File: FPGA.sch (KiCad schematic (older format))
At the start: 8 parts, among them U13 ADS1015, U14 SiT8008B, U8 GW1N-9LQ100

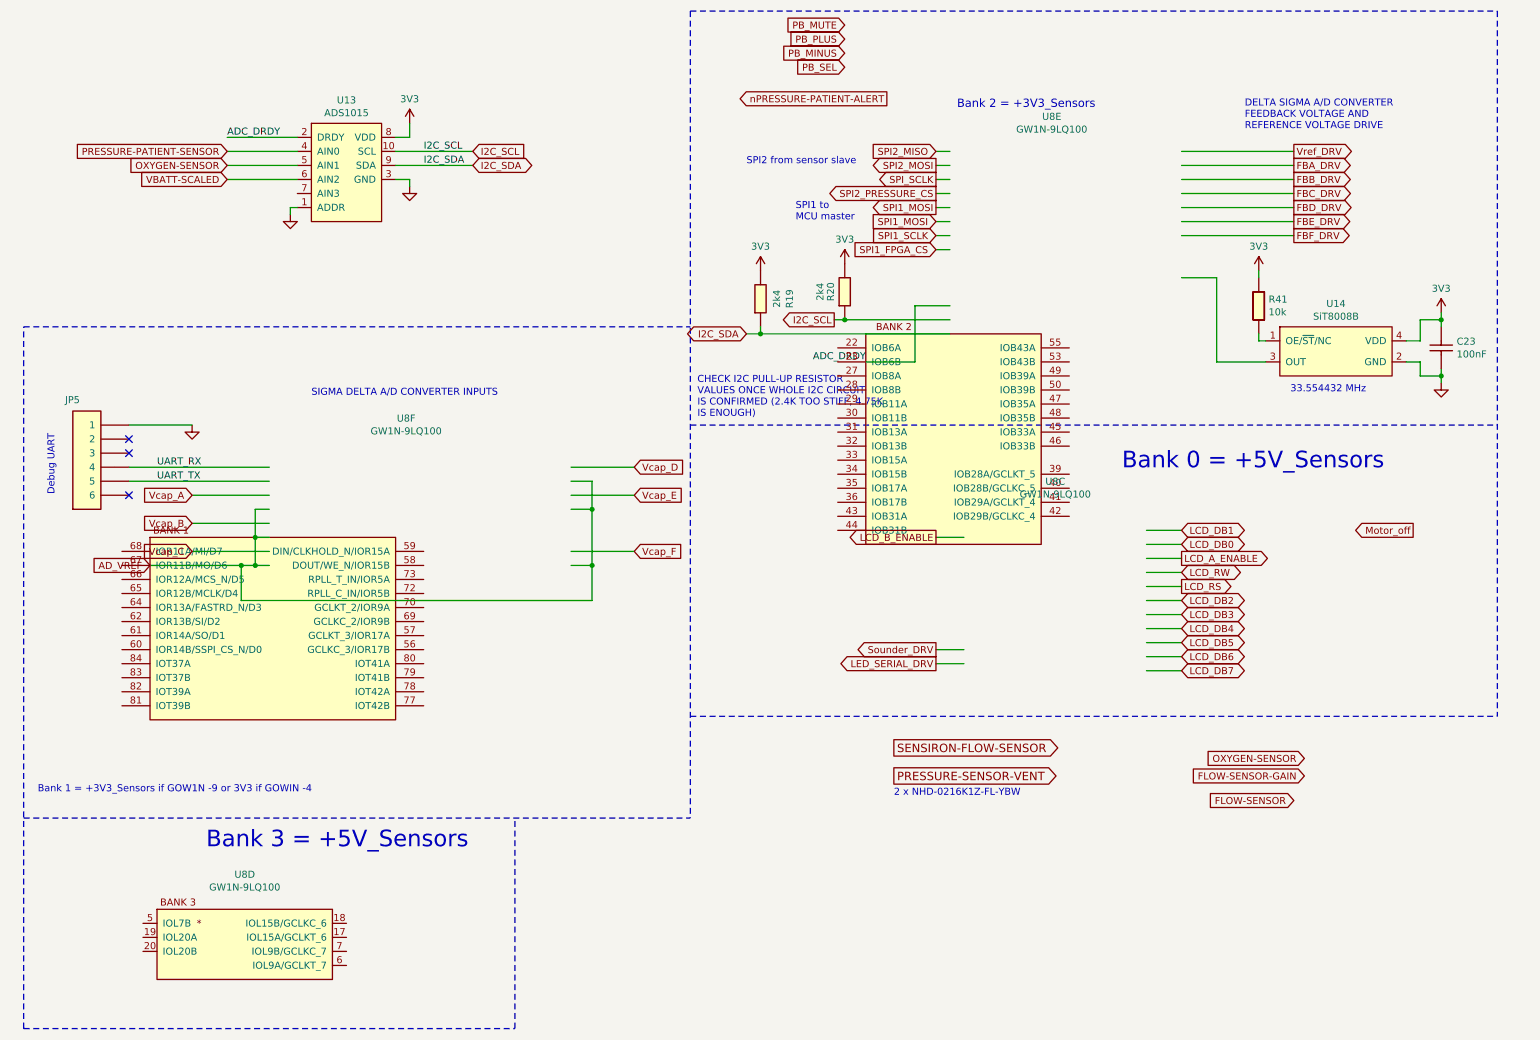
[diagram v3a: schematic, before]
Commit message: Update FPGA symbol, remove FPGA_trial sheet
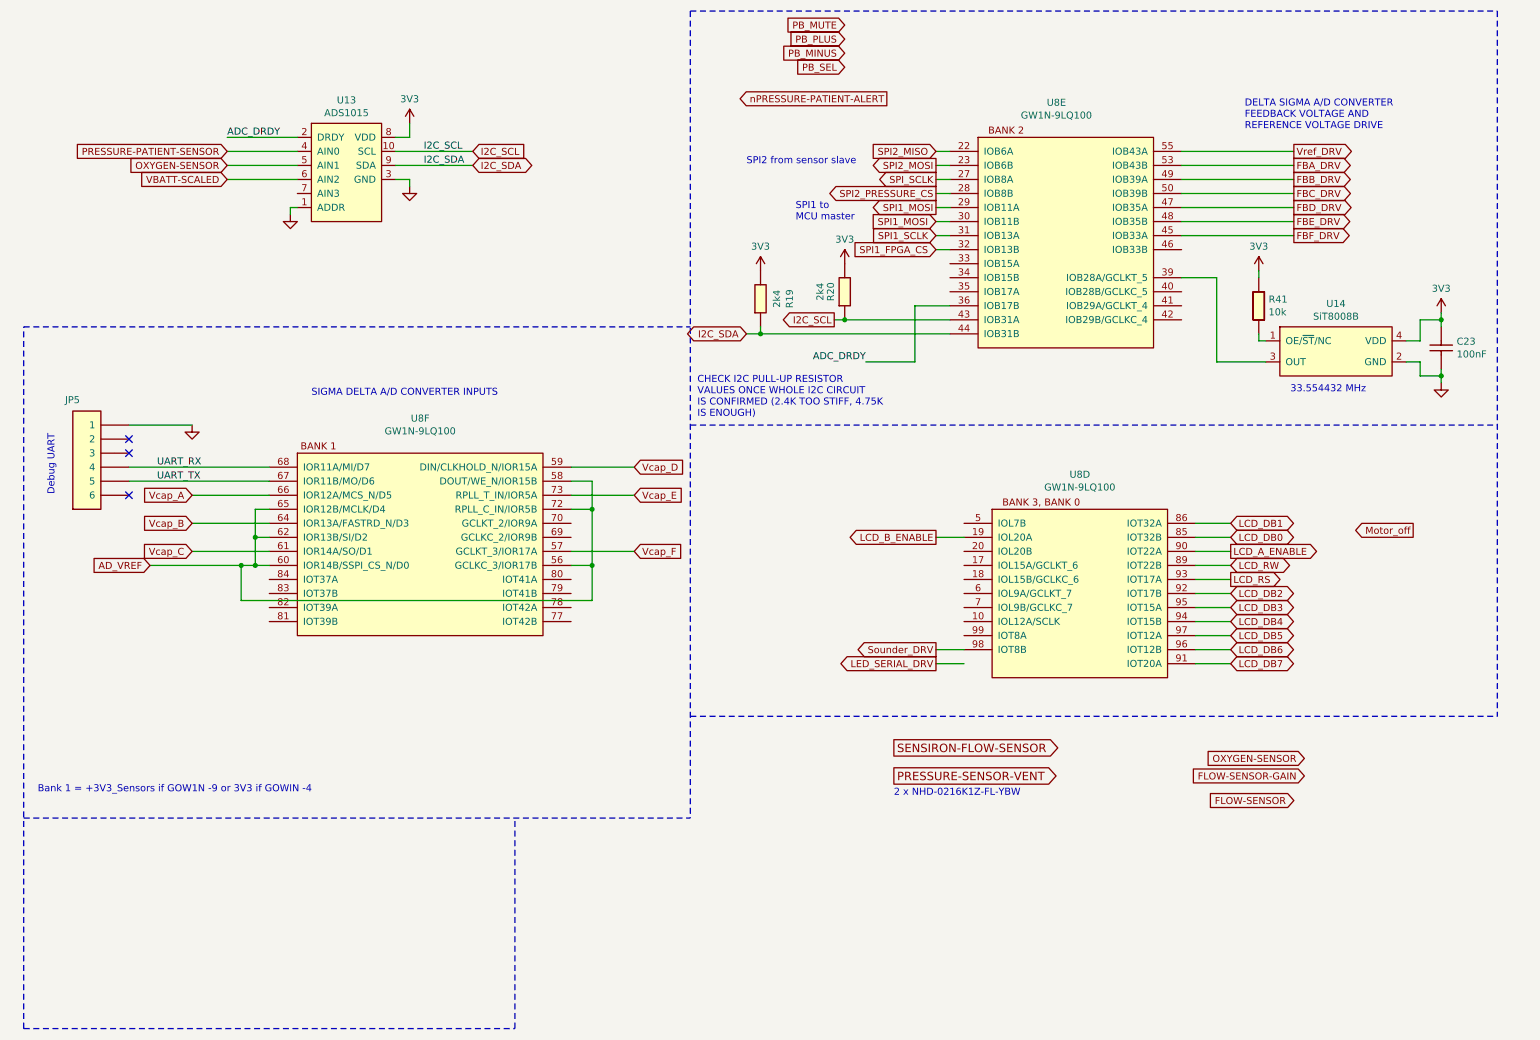
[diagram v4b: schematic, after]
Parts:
- removed unit 4 of U8
- removed unit 3 of U8
- added unit 4 of U8
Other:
- note removed: "Bank 0 = +5V_Sensors"
- note removed: "Bank 2 = +3V3_Sensors\n"
- note removed: "Bank 3 = +5V_Sensors"
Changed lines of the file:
@@
 $Descr A4 11693 8268
 encoding utf-8
-Sheet 6 10
+Sheet 6 9
 Title "OpenVent Control Board"
 Date "2020-10-20"
@@
 PRESSURE-PATIENT-SENSOR
 $Comp
-L OpenVent:GW1N-9LQ100 U8
-U 6 1 5FCFFCE4
-P 2250 4250
-AR Path="/5FCFFCE4" Ref="U8"  Part="6"
-AR Path="/5F8F894A/5FCFFCE4" Ref="U8"  Part="6"
-F 0 "U8" H 3225 5098 50  0000 C CNN
-F 1 "GW1N-9LQ100" H 3225 5007 50  0000 C CNN
-F 2 "" H 2500 6150 50  0001 C CNN
-F 3 "" H 2500 6150 50  0001 C CNN
-	6    2250 4250
-	1    0    0    -1
-$EndComp
-$Comp
-L OpenVent-rescue:GW1N-9LQ100-OpenVent U8
-U 4 1 5FD034FE
-P 1350 7200
-AR Path="/5FD034FE" Ref="U8"  Part="4"
-AR Path="/5F8F894A/5FD034FE" Ref="U8"  Part="4"
-F 0 "U8" H 2075 7748 50  0000 C CNN
-F 1 "GW1N-9LQ100" H 2075 7657 50  0000 C CNN
-F 2 "" H 1600 9100 50  0001 C CNN
-F 3 "" H 1600 9100 50  0001 C CNN
-	4    1350 7200
-	1    0    0    -1
-$EndComp
-$Comp
 L OpenVent:SiT8008B U14
 U 1 1 5FD185A9
@@
 F 3 "" H 5750 2350 50  0001 C CNN
 	1    5750 2350
-	1    0    0    -1
-$EndComp
-$Comp
-L OpenVent:GW1N-9LQ100 U8
-U 5 1 5FE312A6
-P 7100 2800
-AR Path="/5FE312A6" Ref="U8"  Part="5"
-AR Path="/5F8F894A/5FE312A6" Ref="U8"  Part="5"
-F 0 "U8" H 7825 4348 50  0000 C CNN
-F 1 "GW1N-9LQ100" H 7825 4257 50  0000 C CNN
-F 2 "" H 7350 4700 50  0001 C CNN
-F 3 "" H 7350 4700 50  0001 C CNN
-	5    7100 2800
 	1    0    0    -1
 $EndComp
@@
 Text GLabel 4850 4350 2    50   Input ~ 0
 Vcap_F
-Text GLabel 8750 4600 2    50   Output ~ 0
+Text GLabel 9100 4550 2    50   Output ~ 0
 LCD_RS
-Text GLabel 8750 4500 2    50   BiDi ~ 0
+Text GLabel 9100 4450 2    50   BiDi ~ 0
 LCD_RW
-Text GLabel 8750 4400 2    50   Output ~ 0
+Text GLabel 9100 4350 2    50   Output ~ 0
 LCD_A_ENABLE
-Text GLabel 8750 4300 2    50   BiDi ~ 0
+Text GLabel 9100 4250 2    50   BiDi ~ 0
 LCD_DB0
-Text GLabel 8750 4200 2    50   BiDi ~ 0
+Text GLabel 9100 4150 2    50   BiDi ~ 0
 LCD_DB1
-Text GLabel 8750 4800 2    50   BiDi ~ 0
+Text GLabel 9100 4750 2    50   BiDi ~ 0
 LCD_DB3
-Text GLabel 8750 4700 2    50   BiDi ~ 0
+Text GLabel 9100 4650 2    50   BiDi ~ 0
 LCD_DB2
-Text GLabel 8750 5000 2    50   BiDi ~ 0
+Text GLabel 9100 4950 2    50   BiDi ~ 0
 LCD_DB5
-Text GLabel 8750 4900 2    50   BiDi ~ 0
+Text GLabel 9100 4850 2    50   BiDi ~ 0
 LCD_DB4
-Text GLabel 8750 5200 2    50   BiDi ~ 0
+Text GLabel 9100 5150 2    50   BiDi ~ 0
 LCD_DB7
-Text GLabel 8750 5100 2    50   BiDi ~ 0
+Text GLabel 9100 5050 2    50   BiDi ~ 0
 LCD_DB6
 Wire Notes Line
@@
 Wire Notes Line
 	4000 7750 4000 6250
-Text Notes 8325 3775 0    118  ~ 0
-Bank 0 = +5V_Sensors
-Text Notes 7150 1200 0    59   ~ 0
-Bank 2 = +3V3_Sensors\n
-Text Notes 600  6075 0    50   ~ 0
-Bank 1 = +3V3_Sensors if GOW1N -9 or 3V3 if GOWIN -4
-Text Notes 1800 6475 0    118  ~ 0
-Bank 3 = +5V_Sensors
 Wire Notes Line
 	5250 500  11000 500
@@
 $EndComp
 Wire Wire Line
-	8750 4200 8500 4200
-Wire Wire Line
-	8500 4300 8750 4300
-Wire Wire Line
-	8750 4400 8500 4400
-Wire Wire Line
-	8500 4500 8750 4500
-Wire Wire Line
-	8750 4600 8500 4600
-Wire Wire Line
-	8500 4700 8750 4700
-Wire Wire Line
-	8750 4800 8500 4800
-Wire Wire Line
-	8500 4900 8750 4900
-Wire Wire Line
-	8750 5000 8500 5000
-Wire Wire Line
-	8500 5100 8750 5100
-Wire Wire Line
-	8750 5200 8500 5200
+	9100 4150 8850 4150
+Wire Wire Line
+	8850 4250 9100 4250
+Wire Wire Line
+	9100 4350 8850 4350
+Wire Wire Line
+	8850 4450 9100 4450
+Wire Wire Line
+	9100 4550 8850 4550
+Wire Wire Line
+	8850 4650 9100 4650
+Wire Wire Line
+	9100 4750 8850 4750
+Wire Wire Line
+	8850 4850 9100 4850
+Wire Wire Line
+	9100 4950 8850 4950
+Wire Wire Line
+	8850 5050 9100 5050
+Wire Wire Line
+	9100 5150 8850 5150
 Wire Wire Line
 	7200 5050 7000 5050
@@
 Wire Wire Line
 	9000 2400 8750 2400
-$Comp
-L OpenVent:GW1N-9LQ100 U8
-U 3 1 6050EC36
-P 7200 5150
-F 0 "U8" H 7850 6448 50  0000 C CNN
-F 1 "GW1N-9LQ100" H 7850 6357 50  0000 C CNN
-F 2 "" H 6500 6800 50  0001 C CNN
-F 3 "" H 6500 6800 50  0001 C CNN
-	3    7200 5150
-	1    0    0    -1
-$EndComp
 Wire Wire Line
 	1400 4450 2050 4450
@@
 Wire Wire Line
 	7100 2200 7000 2200
+$Comp
+L OpenVent:GW1N-9LQ100 U8
+U 6 1 6053AF87
+P 3300 3650
+F 0 "U8" H 3325 3898 50  0000 C CNN
+F 1 "GW1N-9LQ100" H 3325 3807 50  0000 C CNN
+F 2 "" H 6600 2750 50  0001 C CNN
+F 3 "" H 6600 2750 50  0001 C CNN
+	6    3300 3650
+	1    0    0    -1
+$EndComp
+$Comp
+L OpenVent:GW1N-9LQ100 U8
+U 5 1 6054191D
+P 7900 1400
+F 0 "U8" H 7858 1648 50  0000 C CNN
+F 1 "GW1N-9LQ100" H 7858 1557 50  0000 C CNN
+F 2 "" H 11200 500 50  0001 C CNN
+F 3 "" H 11200 500 50  0001 C CNN
+	5    7900 1400
+	1    0    0    -1
+$EndComp
+$Comp
+L OpenVent:GW1N-9LQ100 U8
+U 4 1 60544613
+P 8050 4050
+F 0 "U8" H 8025 4298 50  0000 C CNN
+F 1 "GW1N-9LQ100" H 8025 4207 50  0000 C CNN
+F 2 "" H 11350 3150 50  0001 C CNN
+F 3 "" H 11350 3150 50  0001 C CNN
+	4    8050 4050
+	1    0    0    -1
+$EndComp
+Text Notes 600  6075 0    50   ~ 0
+Bank 1 = +3V3_Sensors if GOW1N -9 or 3V3 if GOWIN -4
 $EndSCHEMATC

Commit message: Moved UART off FPGA bank 1, attached PB signals to FPGA
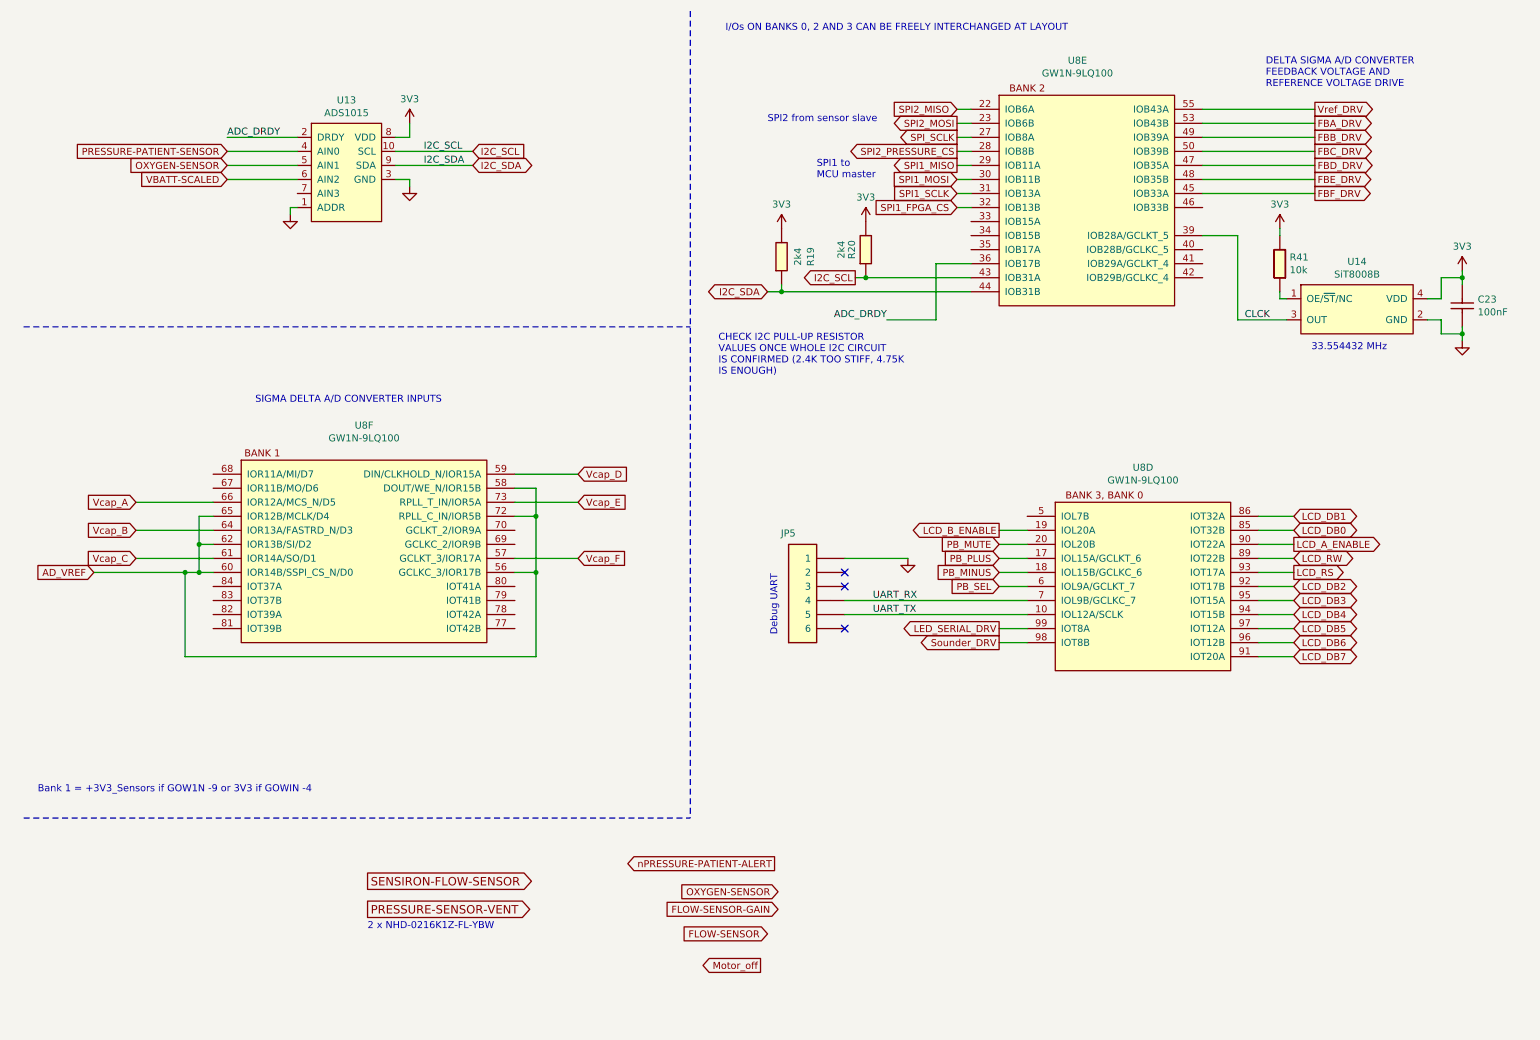
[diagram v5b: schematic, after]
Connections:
- net LED_SERIAL_DRV: now also U8.99 (IOT8A)
- net PB_MINUS: now also U8.18 (IOL15B/GCLKC_6)
- net PB_MUTE: now also U8.20 (IOL20B)
- net PB_PLUS: now also U8.17 (IOL15A/GCLKT_6)
- net PB_SEL: now also U8.6 (IOL9A/GCLKT_7)
- net SPI1_MOSI: no longer U8.29 (IOB11A)
- net UART_RX: now also U8.7 (IOL9B/GCLKC_7); no longer U8.68 (IOR11A/MI/D7)
- net UART_TX: now also U8.10 (IOL12A/SCLK); no longer U8.67 (IOR11B/MO/D6)
- net CLCK: now reaches U14.3 (OUT), U8.39 (IOB28A/GCLKT_5)
- new net SPI1_MISO: U8.29 (IOB11A)
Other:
- note added: "I/Os ON BANKS 0, 2 AND 3 CAN BE FREELY INTERCHANGED AT LAYOUT"
- moved on the sheet: C23, JP5, R19, R20, R41, U14, U8D, U8E, U8F

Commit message: Added FPGA_READY interrupt signal from FPGA to MCU
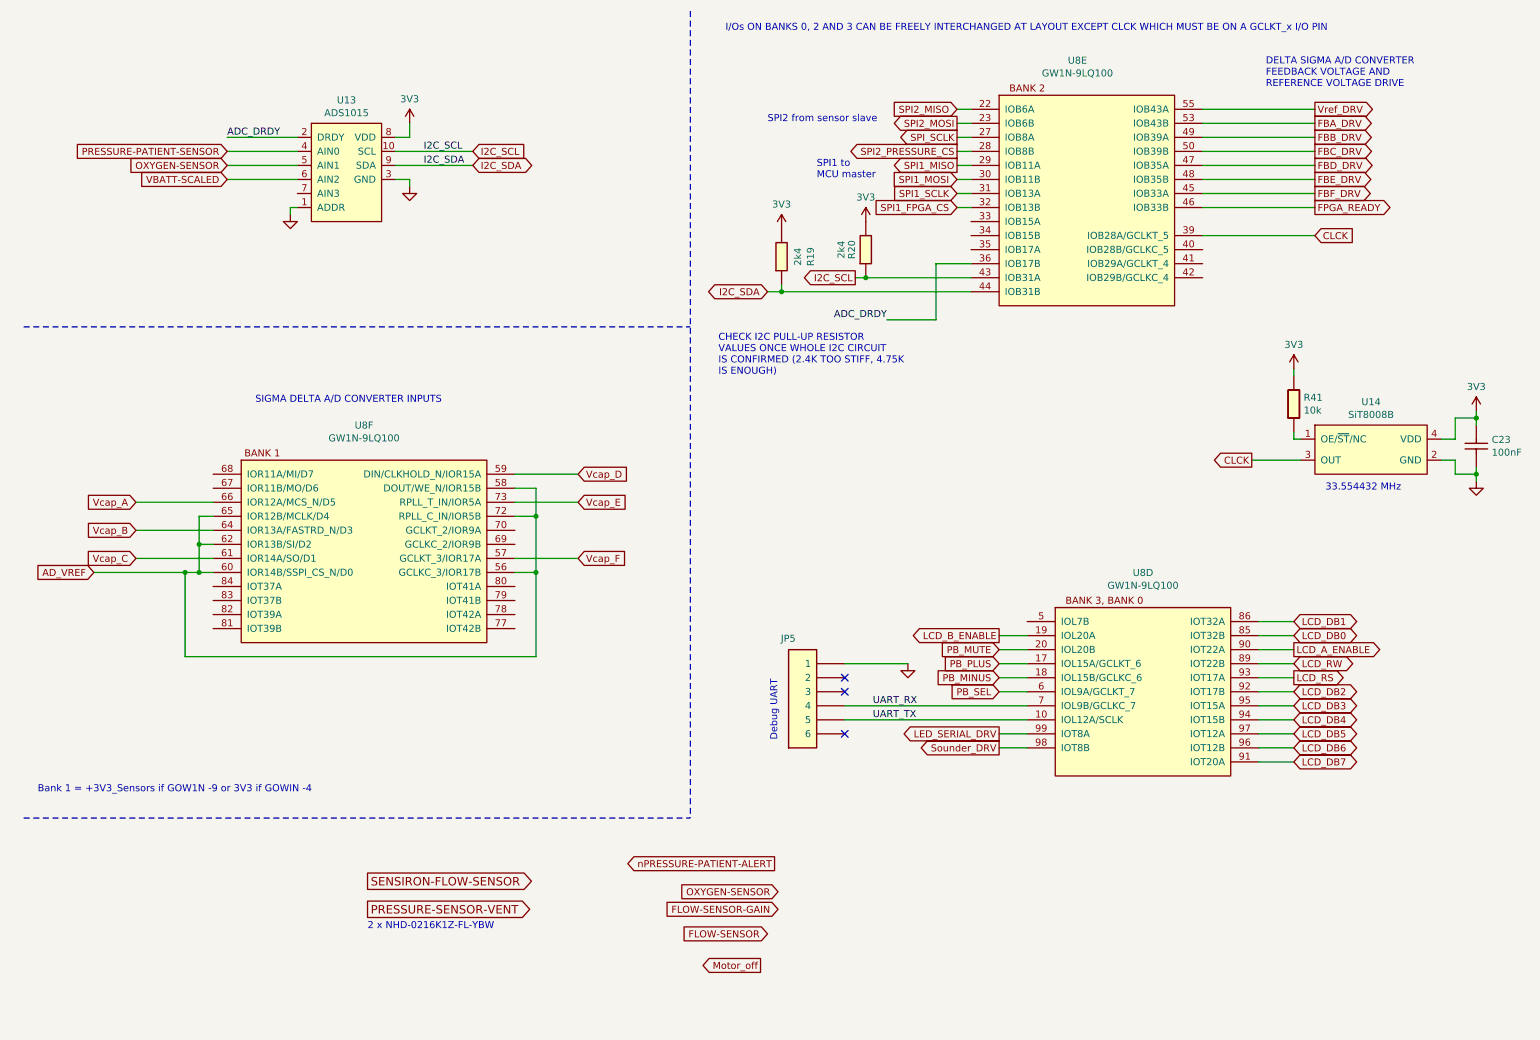
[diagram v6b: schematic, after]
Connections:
- net FPGA_READY: now reaches U8.46 (IOB33B)
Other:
- note added: "I/Os ON BANKS 0, 2 AND 3 CAN BE FREELY INTERCHANGED AT LAYOUT EXCEPT CLCK WHICH MUST BE ON A GCLKT_x I/O PIN"
- note removed: "I/Os ON BANKS 0, 2 AND 3 CAN BE FREELY INTERCHANGED AT LAYOUT"
- moved on the sheet: C23, JP5, R41, U14, U8D
